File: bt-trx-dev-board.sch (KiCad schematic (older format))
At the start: 15 parts, among them J1 RJ45, J2 PTT_BUTTON, J3 PTT_CON, J5 PTT_SELECT, U1 SILabs_WT32i

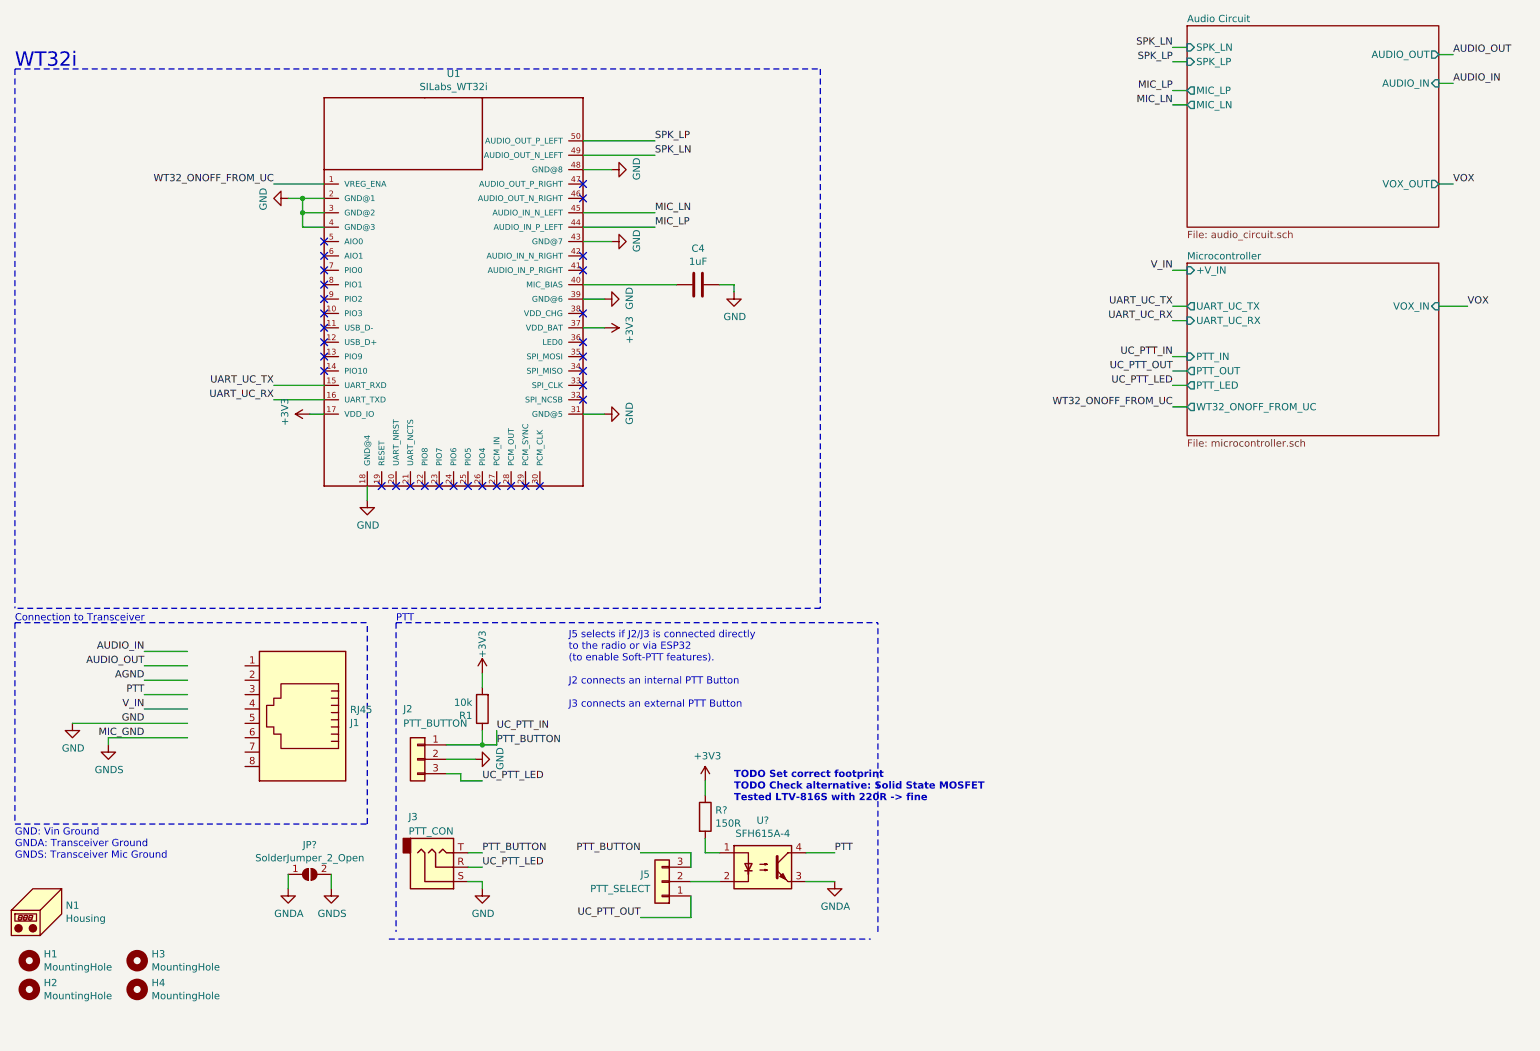
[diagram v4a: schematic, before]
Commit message: Continued Schematic for V5.0
* Rearanged RJ45 connector
* Added jumper wire connector
* Renamed GNDs
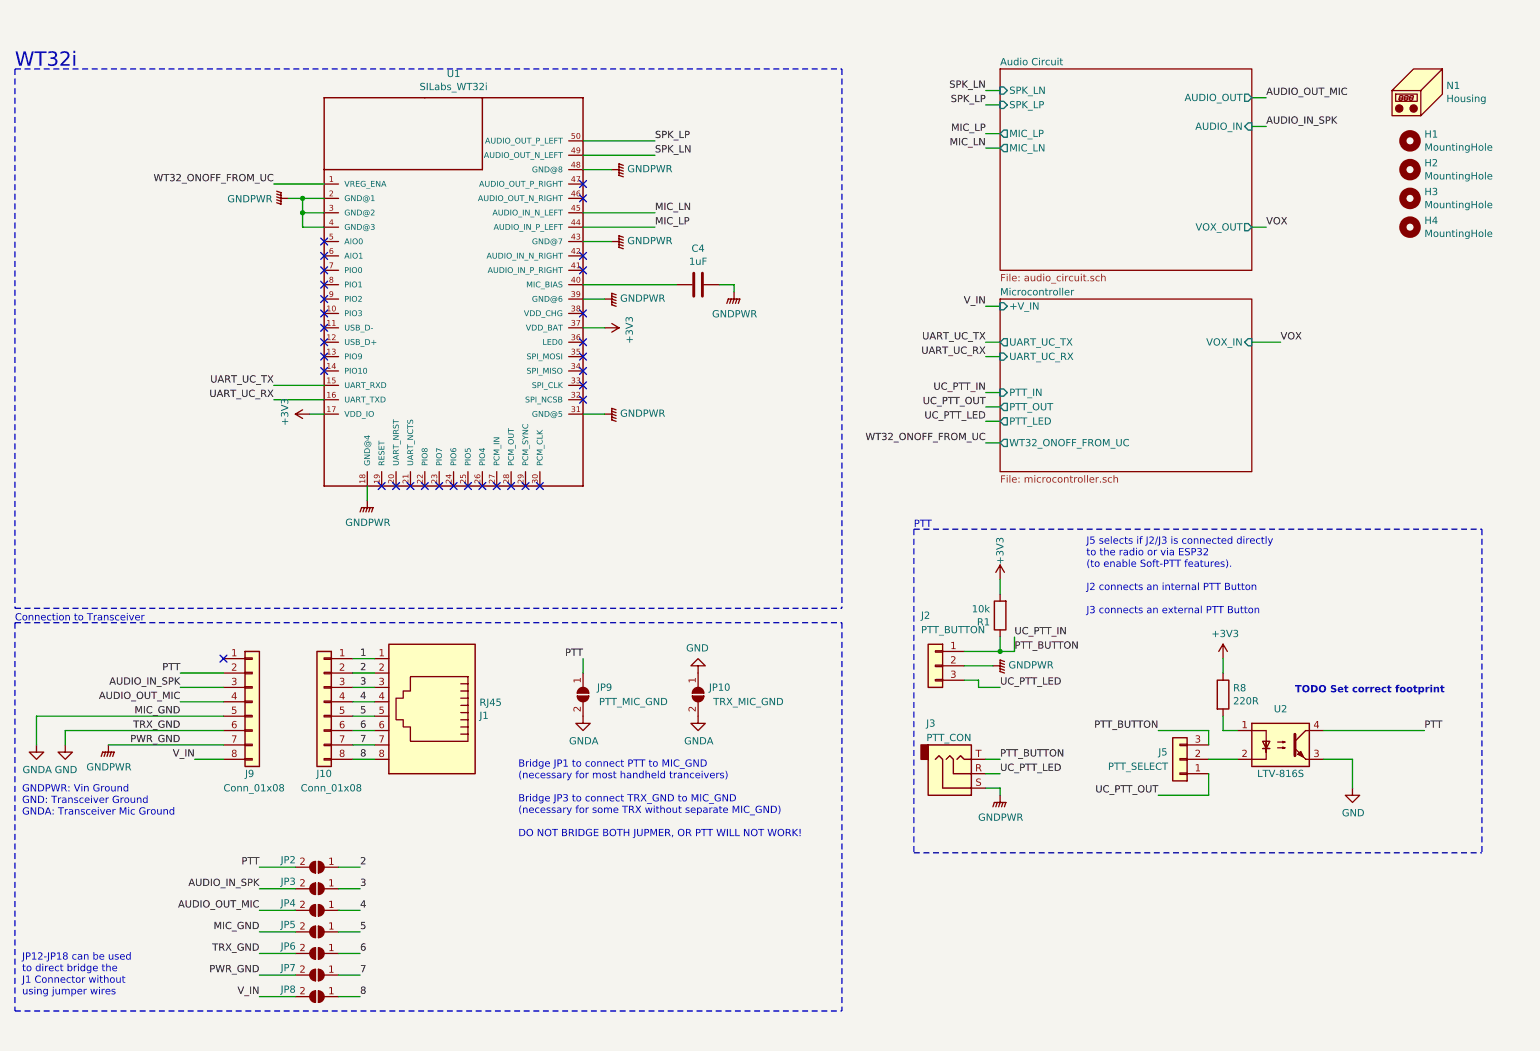
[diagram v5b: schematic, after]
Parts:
- added J10, J9: Conn_01x08, Connector_PinSocket_2.54mm:PinSocket_1x08_P2.54mm_Vertical, symbol Connector_Generic:Conn_01x08
- added JP10: TRX_MIC_GND, Jumper:SolderJumper-2_P1.3mm_Open_TrianglePad1.0x1.5mm, symbol Jumper:SolderJumper_2_Open
- added JP2: 2, Jumper:SolderJumper-2_P1.3mm_Open_TrianglePad1.0x1.5mm, symbol Jumper:SolderJumper_2_Open
- added JP3: 3, Jumper:SolderJumper-2_P1.3mm_Open_TrianglePad1.0x1.5mm, symbol Jumper:SolderJumper_2_Open
- added JP4: 4, Jumper:SolderJumper-2_P1.3mm_Open_TrianglePad1.0x1.5mm, symbol Jumper:SolderJumper_2_Open
- added JP5: 5, Jumper:SolderJumper-2_P1.3mm_Open_TrianglePad1.0x1.5mm, symbol Jumper:SolderJumper_2_Open
- added JP6: 6, Jumper:SolderJumper-2_P1.3mm_Open_TrianglePad1.0x1.5mm, symbol Jumper:SolderJumper_2_Open
- added JP7: 7, Jumper:SolderJumper-2_P1.3mm_Open_TrianglePad1.0x1.5mm, symbol Jumper:SolderJumper_2_Open
- added JP8: 8, Jumper:SolderJumper-2_P1.3mm_Open_TrianglePad1.0x1.5mm, symbol Jumper:SolderJumper_2_Open
- JP9: renamed from JP?; value SolderJumper_2_Open -> PTT_MIC_GND; footprint (none) -> Jumper:SolderJumper-2_P1.3mm_Open_TrianglePad1.0x1.5mm
- R8: renamed from R?; value 150R -> 220R
- U2: renamed from U?; value SFH615A-4 -> LTV-816S; footprint Package_DIP:DIP-4_W7.62mm -> (none)
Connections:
- net labels added: 1, 2, 3, 4, 5, 6, 7, 8, AUDIO_IN_SPK, AUDIO_OUT_MIC, GNDPWR, PWR_GND, TRX_GND
- net labels removed: AGND, AUDIO_IN, AUDIO_OUT, GNDS
- wire segments 71 -> 94
- no-connect marks 32 -> 33
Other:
- note added: "Bridge JP1 to connect PTT to MIC_GND \n(necessary for most handheld tranceivers)\n\nBridge JP3 to connect TRX_GND to MIC_GND \n(necessary for some TRX without separate MIC_GND)\n\nDO NOT BRIDGE BOTH JUPMER, OR PTT WILL NOT WORK!"
- note added: "GNDPWR: Vin Ground\nGND: Transceiver Ground\nGNDA: Transceiver Mic Ground"
- note added: "JP12-JP18 can be used\nto direct bridge the\nJ1 Connector without\nusing jumper wires"
- note added: "TODO Set correct footprint"
- note removed: "GND: Vin Ground\nGNDA: Transceiver Ground\nGNDS: Transceiver Mic Ground"
- note removed: "TODO Set correct footprint\nTODO Check alternative: Solid State MOSFET\nTested LTV-816S with 220R -> fine"
- moved on the sheet: H1, H2, H3, H4, J1, J2, J3, J5, JP9, N1, R1, R8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

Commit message: Replaced PTT-SEL with solder jumper [#21]
* Replaced PTT-SEL with solder jumper
* Fixed typos in comments
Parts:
- removed J5: PTT_SELECT, Connector_PinHeader_2.54mm:PinHeader_1x03_P2.54mm_Vertical, symbol Connector_Generic:Conn_01x03
- added JP11: PTT_SEL, symbol Jumper:SolderJumper_3_Open
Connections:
- net PTT_BUTTON: now also JP11.3 (B)
- net UC_PTT_OUT: now also JP11.1 (A)
- net at U2.2: now also JP11.2 (C)
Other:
- note added: "Bridge JP9 to connect PTT to MIC_GND \n(necessary for most handheld tranceivers)\n\nBridge JP10 to connect TRX_GND to MIC_GND \n(necessary for some TRX without separate MIC_GND)\n\nDO NOT BRIDGE BOTH JUMPER, OR PTT WILL NOT WORK!"
- note added: "JP11 selects if J2/J3 is connected directly\nto the radio or via ESP32\n(to enable Soft-PTT features).\n\nJ2 connects an internal PTT Button\n\nJ3 connects an external PTT Button"
- note removed: "Bridge JP1 to connect PTT to MIC_GND \n(necessary for most handheld tranceivers)\n\nBridge JP3 to connect TRX_GND to MIC_GND \n(necessary for some TRX without separate MIC_GND)\n\nDO NOT BRIDGE BOTH JUPMER, OR PTT WILL NOT WORK!"
- note removed: "J5 selects if J2/J3 is connected directly\nto the radio or via ESP32\n(to enable Soft-PTT features).\n\nJ2 connects an internal PTT Button\n\nJ3 connects an external PTT Button"
- note removed: "TODO Set correct footprint"
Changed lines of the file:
@@
 Wire Wire Line
 	5150 1450 4650 1450
-$Comp
-L Connector_Generic:Conn_01x03 J5
-U 1 1 5C7B53A0
-P 8800 5750
-F 0 "J5" H 8950 5700 50  0000 R CNN
-F 1 "PTT_SELECT" H 9300 5800 50  0000 R CNN
-F 2 "Connector_PinHeader_2.54mm:PinHeader_1x03_P2.54mm_Vertical" H 8800 5750 50  0001 C CNN
-F 3 "~" H 8800 5750 50  0001 C CNN
-F 4 "855-M20-9990346" H 1900 -50 50  0001 C CNN "Mouser Best.Nr."
-	1    8800 5750
-	-1   0    0    1
-$EndComp
-Text Label 8650 6000 2    50   ~ 0
+Text Label 8650 6050 2    50   ~ 0
 UC_PTT_OUT
 Text Label 10500 5550 0    50   ~ 0
@@
 $EndComp
 Text Notes 8150 4750 0    50   ~ 0
-J5 selects if J2/J3 is connected directly\nto the radio or via ESP32\n(to enable Soft-PTT features).\n\nJ2 connects an internal PTT Button\n\nJ3 connects an external PTT Button
+JP11 selects if J2/J3 is connected directly\nto the radio or via ESP32\n(to enable Soft-PTT features).\n\nJ2 connects an internal PTT Button\n\nJ3 connects an external PTT Button
 $Comp
 L Mechanical:MountingHole H3
@@
 	9000 5750 9200 5750
 Wire Wire Line
-	8650 6000 9000 6000
-Wire Wire Line
-	9000 6000 9000 5850
-Wire Wire Line
 	7300 5100 7500 5100
 Wire Wire Line
@@
 Wire Wire Line
 	7450 5750 7550 5750
-Text Label 8650 5550 2    50   ~ 0
+Text Label 8650 5450 2    50   ~ 0
 PTT_BUTTON
-Wire Wire Line
-	8650 5550 9000 5550
-Wire Wire Line
-	9000 5550 9000 5650
 Wire Wire Line
 	7550 4500 7550 4600
@@
 Wire Wire Line
 	9800 5750 10000 5750
-Text Notes 9600 5300 0    50   ~ 10
-TODO Set correct footprint
 Text Label 7650 4900 0    50   ~ 0
 UC_PTT_IN
@@
 	4650 5050 4650 5150
 Text Notes 4200 6300 0    50   ~ 0
-Bridge JP1 to connect PTT to MIC_GND \n(necessary for most handheld tranceivers)\n\nBridge JP3 to connect TRX_GND to MIC_GND \n(necessary for some TRX without separate MIC_GND)\n\nDO NOT BRIDGE BOTH JUPMER, OR PTT WILL NOT WORK!
+Bridge JP9 to connect PTT to MIC_GND \n(necessary for most handheld tranceivers)\n\nBridge JP10 to connect TRX_GND to MIC_GND \n(necessary for some TRX without separate MIC_GND)\n\nDO NOT BRIDGE BOTH JUMPER, OR PTT WILL NOT WORK!
 $Comp
 L power:GND #PWR02
@@
 Wire Notes Line
 	700  950  6450 950
+$Comp
+L Jumper:SolderJumper_3_Open JP11
+U 1 1 5E77194E
+P 8850 5750
+F 0 "JP11" V 8896 5818 50  0000 L CNN
+F 1 "PTT_SEL" V 8805 5818 50  0000 L CNN
+F 2 "" H 8850 5750 50  0001 C CNN
+F 3 "~" H 8850 5750 50  0001 C CNN
+	1    8850 5750
+	0    -1   -1   0
+$EndComp
+Wire Wire Line
+	8650 5450 8850 5450
+Wire Wire Line
+	8850 5450 8850 5550
+Wire Wire Line
+	8850 5950 8850 6050
+Wire Wire Line
+	8850 6050 8650 6050
 $EndSCHEMATC

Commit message: Fixed Typos and Missing Footprints [#21]
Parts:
- JP11: footprint (none) -> Jumper:SolderJumper-3_P2.0mm_Open_TrianglePad1.0x1.5mm
- U2: footprint (none) -> liteon:LTV-816S
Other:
- note added: "Bridge JP9 to connect PTT to MIC_GND \n(necessary for most handheld transceivers)\n\nBridge JP10 to connect TRX_GND to MIC_GND \n(necessary for some TRX without separate MIC_GND)\n\nDO NOT BRIDGE BOTH JUMPER, OR PTT WILL NOT WORK!"
- note added: "JP2-JP8 can be used\nto direct bridge the\nJ9/J10 Connectors without\nusing jumper wires"
- note removed: "Bridge JP9 to connect PTT to MIC_GND \n(necessary for most handheld tranceivers)\n\nBridge JP10 to connect TRX_GND to MIC_GND \n(necessary for some TRX without separate MIC_GND)\n\nDO NOT BRIDGE BOTH JUMPER, OR PTT WILL NOT WORK!"
- note removed: "JP12-JP18 can be used\nto direct bridge the\nJ1 Connector without\nusing jumper wires"
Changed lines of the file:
@@
 F 0 "U2" H 9500 5900 50  0000 C CNN
 F 1 "LTV-816S" H 9500 5450 50  0000 C CNN
-F 2 "" H 9300 5450 50  0001 L CIN
+F 2 "liteon:LTV-816S" H 9300 5450 50  0001 L CIN
 F 3 "https://www.mouser.de/datasheet/2/239/LTV-8x6-1175385.pdf" H 9500 5650 50  0001 L CNN
 	1    9500 5650
@@
 	4650 5050 4650 5150
 Text Notes 4200 6300 0    50   ~ 0
-Bridge JP9 to connect PTT to MIC_GND \n(necessary for most handheld tranceivers)\n\nBridge JP10 to connect TRX_GND to MIC_GND \n(necessary for some TRX without separate MIC_GND)\n\nDO NOT BRIDGE BOTH JUMPER, OR PTT WILL NOT WORK!
+Bridge JP9 to connect PTT to MIC_GND \n(necessary for most handheld transceivers)\n\nBridge JP10 to connect TRX_GND to MIC_GND \n(necessary for some TRX without separate MIC_GND)\n\nDO NOT BRIDGE BOTH JUMPER, OR PTT WILL NOT WORK!
 $Comp
 L power:GND #PWR02
@@
 	2400 7400 2650 7400
 Text Notes 750  7400 0    50   ~ 0
-JP12-JP18 can be used\nto direct bridge the\nJ1 Connector without\nusing jumper wires
+JP2-JP8 can be used\nto direct bridge the\nJ9/J10 Connectors without\nusing jumper wires
 Wire Notes Line
 	700  7500 6450 7500
@@
 F 0 "JP11" V 8896 5818 50  0000 L CNN
 F 1 "PTT_SEL" V 8805 5818 50  0000 L CNN
-F 2 "" H 8850 5750 50  0001 C CNN
+F 2 "Jumper:SolderJumper-3_P2.0mm_Open_TrianglePad1.0x1.5mm" H 8850 5750 50  0001 C CNN
 F 3 "~" H 8850 5750 50  0001 C CNN
 	1    8850 5750
